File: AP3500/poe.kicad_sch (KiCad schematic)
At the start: 72 parts, among them IC2 TPS23751PWPR, J11 Barrel_Jack, Q1 FDS86242, U12 HMHA2801AR2, U6 TL431AIDBVR

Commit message: Finalize AP3500 board
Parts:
- removed TP11, TP9: TestPoint, TestPoint:TestPoint_Keystone_5000-5004_Miniature, symbol Connector:TestPoint
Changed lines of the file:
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@@
   (junction (at 256.54 83.82) (diameter 1.016) (color 0 0 0 0))
   (junction (at 256.54 100.33) (diameter 1.016) (color 0 0 0 0))
-  (junction (at 259.08 83.82) (diameter 1.016) (color 0 0 0 0))
-  (junction (at 259.08 100.33) (diameter 1.016) (color 0 0 0 0))
   (junction (at 267.97 83.82) (diameter 1.016) (color 0 0 0 0))
   (no_connect (at 41.91 143.51))
@@
     (stroke (width 0) (type solid) (color 0 0 0 0))
   )
-  (wire (pts (xy 256.54 83.82) (xy 259.08 83.82))
+  (wire (pts (xy 256.54 83.82) (xy 267.97 83.82))
     (stroke (width 0) (type solid) (color 0 0 0 0))
   )
@@
     (stroke (width 0) (type solid) (color 0 0 0 0))
   )
-  (wire (pts (xy 256.54 100.33) (xy 259.08 100.33))
-    (stroke (width 0) (type solid) (color 0 0 0 0))
-  )
-  (wire (pts (xy 259.08 83.82) (xy 267.97 83.82))
-    (stroke (width 0) (type solid) (color 0 0 0 0))
-  )
-  (wire (pts (xy 259.08 100.33) (xy 264.16 100.33))
+  (wire (pts (xy 256.54 100.33) (xy 264.16 100.33))
     (stroke (width 0) (type solid) (color 0 0 0 0))
   )
@@
     (effects (font (size 2.007 2.007)) (justify left))
   )
-  (symbol (lib_id "Connector:TestPoint") (at 259.08 83.82 0) (unit 1)
-    (in_bom yes) (on_board yes)
-    (property "Reference" "TP9" (id 0) (at 260.5532 80.8228 0)
-      (effects (font (size 1.27 1.27)) (justify left))
-    )
-    (property "Value" "TestPoint" (id 1) (at 260.5532 83.1342 0)
-      (effects (font (size 1.27 1.27)) (justify left) hide)
-    )
-    (property "Footprint" "TestPoint:TestPoint_Keystone_5000-5004_Miniature" (id 2) (at 264.16 83.82 0)
-      (effects (font (size 1.27 1.27)) hide)
-    )
-    (property "Datasheet" "" (id 3) (at 264.16 83.82 0)
-      (effects (font (size 1.27 1.27)) hide)
-    )
-    (property "Field4" "nf" (id 4) (at 259.08 83.82 0)
-      (effects (font (size 1.27 1.27)) hide)
-    )
-    (property "Field5" "nf" (id 5) (at 259.08 83.82 0)
-      (effects (font (size 1.27 1.27)) hide)
-    )
-    (property "Field6" "nf" (id 6) (at 259.08 83.82 0)
-      (effects (font (size 1.27 1.27)) hide)
-    )
-    (property "Field7" "nf" (id 7) (at 259.08 83.82 0)
-      (effects (font (size 1.27 1.27)) hide)
-    )
-    (property "PartsBoxID" "5001" (id 4) (at 259.08 83.82 0)
-      (effects (font (size 1.27 1.27)) hide)
-    )
-  )
-  (symbol (lib_id "Connector:TestPoint") (at 259.08 100.33 180) (unit 1)
-    (in_bom yes) (on_board yes)
-    (property "Reference" "TP11" (id 0) (at 257.6068 103.3272 0)
-      (effects (font (size 1.27 1.27)) (justify left))
-    )
-    (property "Value" "TestPoint" (id 1) (at 257.6068 101.0158 0)
-      (effects (font (size 1.27 1.27)) (justify left) hide)
-    )
-    (property "Footprint" "TestPoint:TestPoint_Keystone_5000-5004_Miniature" (id 2) (at 254 100.33 0)
-      (effects (font (size 1.27 1.27)) hide)
-    )
-    (property "Datasheet" "" (id 3) (at 254 100.33 0)
-      (effects (font (size 1.27 1.27)) hide)
-    )
-    (property "Field4" "nf" (id 4) (at 259.08 100.33 0)
-      (effects (font (size 1.27 1.27)) hide)
-    )
-    (property "Field5" "nf" (id 5) (at 259.08 100.33 0)
-      (effects (font (size 1.27 1.27)) hide)
-    )
-    (property "Field6" "nf" (id 6) (at 259.08 100.33 0)
-      (effects (font (size 1.27 1.27)) hide)
-    )
-    (property "Field7" "nf" (id 7) (at 259.08 100.33 0)
-      (effects (font (size 1.27 1.27)) hide)
-    )
-    (property "PartsBoxID" "5001" (id 4) (at 259.08 100.33 0)
-      (effects (font (size 1.27 1.27)) hide)
-    )
-  )
   (symbol (lib_id "power:GNDPWR") (at 29.21 153.67 0) (unit 1)

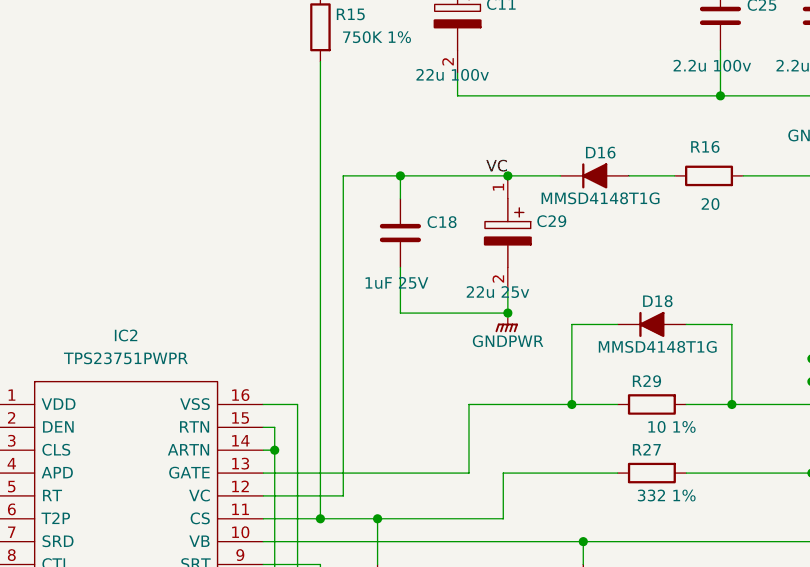
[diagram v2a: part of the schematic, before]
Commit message: More work on Antennas - laying out the new panel as a 2x2 aperture coupled patch
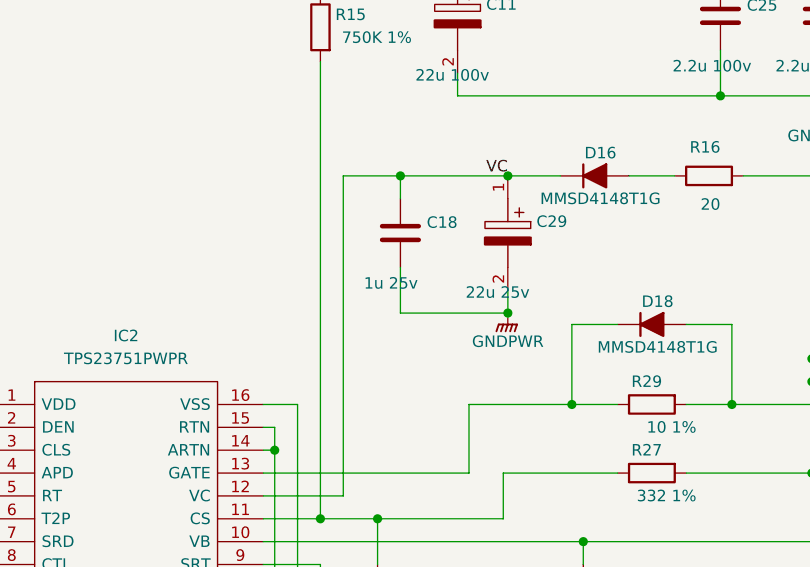
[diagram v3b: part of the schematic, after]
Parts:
- C10, C25: LCSC (none) -> C76685
- C11: LCSC (none) -> C249491; PartsBoxID EEE-FK2A220P -> AEC-SMD-8mm-22uF-100VDC-20%
- C12, C13, C14, C15: footprint Capacitor_SMD:C_1210_3225Metric -> Capacitor_SMD:C_1206_3216Metric; LCSC (none) -> C90146; PartsBoxID 1210-22uF-X7R-16V -> 1206-22uF-X7R-16V
- C18: value 1uF 25V -> 1u 25v; LCSC (none) -> C89190; PartsBoxID 0805-1uF-X5R-25V -> 0805-1uF-X7R-25V
- C26: LCSC (none) -> C14858
- C27, C8: LCSC (none) -> C15725
- C28: LCSC (none) -> C173219
- C29: LCSC (none) -> C336292
- C32: LCSC (none) -> C1623
- C33: LCSC (none) -> C1664
- C34: LCSC (none) -> C21117
- C36: LCSC (none) -> C89190
- C38: LCSC (none) -> C21122
- C4, C5, C6, C7: LCSC (none) -> C15177
- C9: LCSC (none) -> C22423
- D10, D11, D12, D13, D4, D5, D6, D7, D8: LCSC (none) -> C526416
- D16, D18: LCSC (none) -> C132796
- D17: LCSC (none) -> C83935
- D9: LCSC (none) -> C115922
- Q1: LCSC (none) -> C113197
- R11: LCSC (none) -> C25803
- R12: LCSC (none) -> C23043
- R13: LCSC (none) -> C25826
- R14: LCSC (none) -> C25962
- R15: LCSC (none) -> C23240
- R16: LCSC (none) -> C17544
- R17: LCSC (none) -> C21189
- R18: LCSC (none) -> C23223
- R21, R26: LCSC (none) -> C25804
- R22: LCSC (none) -> C21190
- R23: LCSC (none) -> C23008
- R24, R25, R34: LCSC (none) -> C22975
- R27: LCSC (none) -> C23007
- R29: LCSC (none) -> C22859
- R31: LCSC (none) -> C247543
- R35: LCSC (none) -> C22942
- R4: LCSC (none) -> C35217
- R5: LCSC (none) -> C23046
- TR1: LCSC (none) -> C465989; PartsBoxID TSE265 -> C465989
- U12: LCSC (none) -> C258257
- U6: LCSC (none) -> C144392

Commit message: Add new single polarity aperture coupled 4x4 antenna. RasPiCNM4Connector test Gerbers for PCBWay Cleanups and optimixations for AP3500
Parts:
- C10, C25: PartsBoxID 1210-2.2uF-X7R-100V -> (none)
- C12, C13, C14, C15: PartsBoxID 1206-22uF-X7R-16V -> (none)
- C18, C36: PartsBoxID 0805-1uF-X7R-25V -> (none)
- C26: PartsBoxID GRM1885C1H101JA01D -> (none)
- C27, C8: PartsBoxID 0603-100nF-X7R-100V -> (none)
- C32: PartsBoxID 0603-.47uF-X7R-16V -> (none)
- C33: PartsBoxID 0603-330pF-C0G-50V -> (none)
- C34: PartsBoxID 0603-33nF-X7R-25V -> (none)
- C38: PartsBoxID 0603-22nF-X7R-50V -> (none)
- C4, C5, C6, C7: PartsBoxID 0805-1000pF-X7R-100V -> (none)
- C9: PartsBoxID 0603-2200pF-X7R-100V -> (none)
- R11: PartsBoxID 0603-100K-1% -> (none)
- R12: PartsBoxID 0603-4.42K-1% -> (none)
- R13: PartsBoxID 0805-39K-1%-250mW -> (none)
- R14: PartsBoxID 0603-24.9K-1% -> (none)
- R15: PartsBoxID 0603-750K-1% -> (none)
- R17: PartsBoxID 0603-0R-1% -> (none)
- R18: PartsBoxID 0603-63.4-1%-100mW -> (none)
- R21, R26: PartsBoxID 0603-10K-1% -> (none)
- R22: PartsBoxID 0603-1K-1% -> (none)
- R23: PartsBoxID 0603-34K-1% -> (none)
- R24, R25, R34: PartsBoxID 0603-2K-1% -> (none)
- R27: PartsBoxID 0603-332-1% -> (none)
- R29: PartsBoxID CRCW060310R0JNEA -> (none)
- R31: PartsBoxID KDV12FR082ET -> (none)
- R35: PartsBoxID 0603-2.61K-1% -> (none)
- R4: PartsBoxID CRCW25127R50JNEG -> (none)
- R5: PartsBoxID CRCW06034K99FKEA -> (none)

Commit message: Rework AP3500
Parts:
- TR1: footprint Scott:Transformer_TNK_TSE265 -> Scott:Transformer_Dual_TNK_TSE265_Wurth
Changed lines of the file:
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@@
     (property "Reference" "TR1" (id 0) (at 187.96 67.31 0))
     (property "Value" "TSE265  /  C465989" (id 1) (at 187.96 69.85 0))
-    (property "Footprint" "Scott:Transformer_TNK_TSE265" (id 2) (at 186.69 86.36 0)
+    (property "Footprint" "Scott:Transformer_Dual_TNK_TSE265_Wurth" (id 2) (at 186.69 86.36 0)
       (effects (font (size 1.27 1.27)) hide)
     )

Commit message: Updates for JLCPCB components actually in stock at this time
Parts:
- C10, C25: LCSC C76685 -> C55151
- C29: footprint Capacitor_SMD:CP_Elec_5x5.8 -> Capacitor_SMD:CP_Elec_5x5.4; LCSC C336292 -> C239255
- D17: LCSC C83935 -> C47546
- FB1, FB2, FB3, FB4: footprint Inductor_SMD:L_0603_1608Metric -> Inductor_SMD:L_0805_2012Metric; LCSC (none) -> C56066
- Q1: LCSC C113197 -> C57665
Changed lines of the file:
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@@
-(kicad_sch (version 20210406) (generator eeschema)
+(kicad_sch (version 20210606) (generator eeschema)
   (paper "A4")
   (title_block
@@
     (property "Reference" "FB1" (id 0) (at 110.49 23.495 90))
     (property "Value" "300 OHM" (id 1) (at 110.49 26.67 90))
-    (property "Footprint" "Inductor_SMD:L_0603_1608Metric" (id 2) (at 110.49 25.4 0)
+    (property "Footprint" "Inductor_SMD:L_0805_2012Metric" (id 2) (at 110.49 25.4 0)
       (effects (font (size 1.27 1.27)) hide)
     )
@@
       (effects (font (size 1.27 1.27)) hide)
     )
+    (property "LCSC" "C56066" (id 5) (at 110.49 25.4 0)
+      (effects (font (size 1.27 1.27)) hide)
+    )
     (pin "1")
     (pin "2")
@@
     (property "Reference" "FB4" (id 0) (at 110.49 51.435 90))
     (property "Value" "300 OHM" (id 1) (at 110.49 54.61 90))
-    (property "Footprint" "Inductor_SMD:L_0603_1608Metric" (id 2) (at 110.49 53.34 0)
+    (property "Footprint" "Inductor_SMD:L_0805_2012Metric" (id 2) (at 110.49 53.34 0)
       (effects (font (size 1.27 1.27)) hide)
     )
@@
       (effects (font (size 1.27 1.27)) hide)
     )
+    (property "LCSC" "C56066" (id 5) (at 110.49 53.34 0)
+      (effects (font (size 1.27 1.27)) hide)
+    )
     (pin "1")
     (pin "2")
@@
     (property "Reference" "FB2" (id 0) (at 201.93 23.495 90))
     (property "Value" "300 OHM" (id 1) (at 201.93 26.67 90))
-    (property "Footprint" "Inductor_SMD:L_0603_1608Metric" (id 2) (at 201.93 25.4 0)
+    (property "Footprint" "Inductor_SMD:L_0805_2012Metric" (id 2) (at 201.93 25.4 0)
       (effects (font (size 1.27 1.27)) hide)
     )
@@
       (effects (font (size 1.27 1.27)) hide)
     )
+    (property "LCSC" "C56066" (id 5) (at 201.93 25.4 0)
+      (effects (font (size 1.27 1.27)) hide)
+    )
     (pin "1")
     (pin "2")
@@
     (property "Reference" "FB3" (id 0) (at 201.93 47.625 90))
     (property "Value" "300 OHM" (id 1) (at 201.93 50.8 90))
-    (property "Footprint" "Inductor_SMD:L_0603_1608Metric" (id 2) (at 201.93 49.53 0)
+    (property "Footprint" "Inductor_SMD:L_0805_2012Metric" (id 2) (at 201.93 49.53 0)
       (effects (font (size 1.27 1.27)) hide)
     )
@@
       (effects (font (size 1.27 1.27)) hide)
     )
+    (property "LCSC" "C56066" (id 5) (at 201.93 49.53 0)
+      (effects (font (size 1.27 1.27)) hide)
+    )
     (pin "1")
     (pin "2")
@@
       (effects (font (size 1.27 1.27)) hide)
     )
-    (property "LCSC" "C76685" (id 10) (at 123.19 85.09 0)
+    (property "LCSC" "C55151" (id 10) (at 123.19 85.09 0)
       (effects (font (size 1.27 1.27)) hide)
     )
@@
       (effects (font (size 1.27 1.27)) hide)
     )
-    (property "LCSC" "C76685" (id 10) (at 134.62 85.09 0)
+    (property "LCSC" "C55151" (id 10) (at 134.62 85.09 0)
       (effects (font (size 1.27 1.27)) hide)
     )
@@
       (effects (font (size 1.27 1.27)) (justify left))
     )
-    (property "Footprint" "Capacitor_SMD:CP_Elec_5x5.8" (id 2) (at 100.838 111.76 0)
+    (property "Footprint" "Capacitor_SMD:CP_Elec_5x5.4" (id 2) (at 100.838 111.76 0)
       (effects (font (size 1.27 1.27)) (justify left) hide)
     )
@@
       (effects (font (size 1.27 1.27)) (justify left) hide)
     )
-    (property "LCSC" "C336292" (id 12) (at 99.568 102.87 0)
+    (property "LCSC" "C239255" (id 12) (at 99.568 102.87 0)
       (effects (font (size 1.27 1.27)) hide)
     )
@@
       (effects (font (size 1.27 1.27)) hide)
     )
-    (property "LCSC" "C83935" (id 5) (at 219.71 129.54 0)
+    (property "LCSC" "C47546" (id 5) (at 219.71 129.54 0)
       (effects (font (size 1.27 1.27)) hide)
     )
@@
       (effects (font (size 1.27 1.27)) (justify left) hide)
     )
-    (property "LCSC" "C113197" (id 12) (at 139.7 120.65 0)
+    (property "LCSC" "C57665" (id 12) (at 139.7 120.65 0)
       (effects (font (size 1.27 1.27)) hide)
     )

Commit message: Update AP3500 with new Wurth footprint - needed rerouted. Fix the gigabit ethernet problem with pair 4 center tap to ground instead of through cap.
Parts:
- TR1: footprint Scott:Transformer_Dual_TNK_TSE265_Wurth -> Scott:Transformer_EP13
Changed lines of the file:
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@@
-(kicad_sch (version 20210606) (generator eeschema)
+(kicad_sch (version 20210621) (generator eeschema)
   (paper "A4")
   (title_block
@@
     (property "Reference" "TR1" (id 0) (at 187.96 67.31 0))
     (property "Value" "TSE265  /  C465989" (id 1) (at 187.96 69.85 0))
-    (property "Footprint" "Scott:Transformer_Dual_TNK_TSE265_Wurth" (id 2) (at 186.69 86.36 0)
+    (property "Footprint" "Scott:Transformer_EP13" (id 2) (at 186.69 86.36 0)
       (effects (font (size 1.27 1.27)) hide)
     )
